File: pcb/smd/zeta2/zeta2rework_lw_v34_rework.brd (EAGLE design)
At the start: 81 x 50.2 mm, 92 parts, among them IC1 DRV8844PWPR, IC2 DRV8844PWPR, M1 IRLML2502, M2 IRLML2502, M3 IRLML2502, U1 STM32F427VI, U3 ICM-20948, U5 DS18B20U+

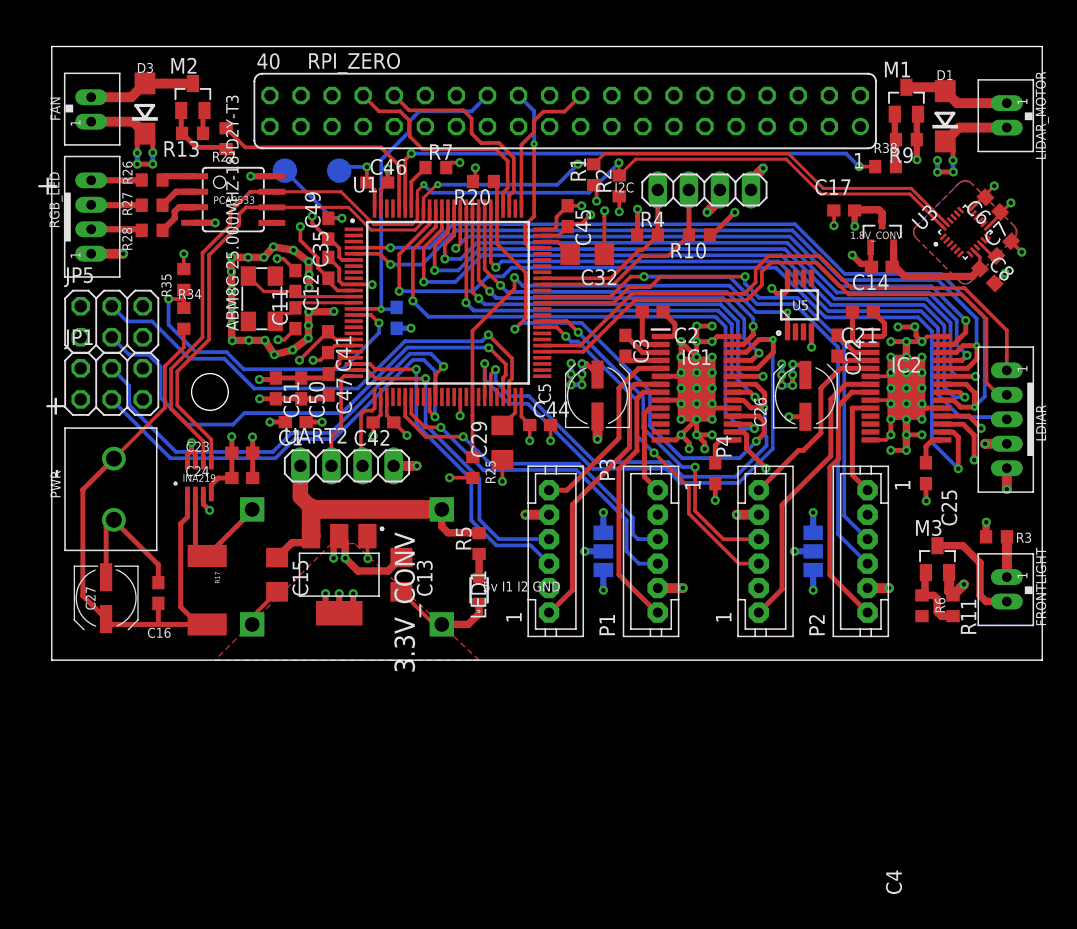
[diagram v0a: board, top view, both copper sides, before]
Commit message: connected power supply
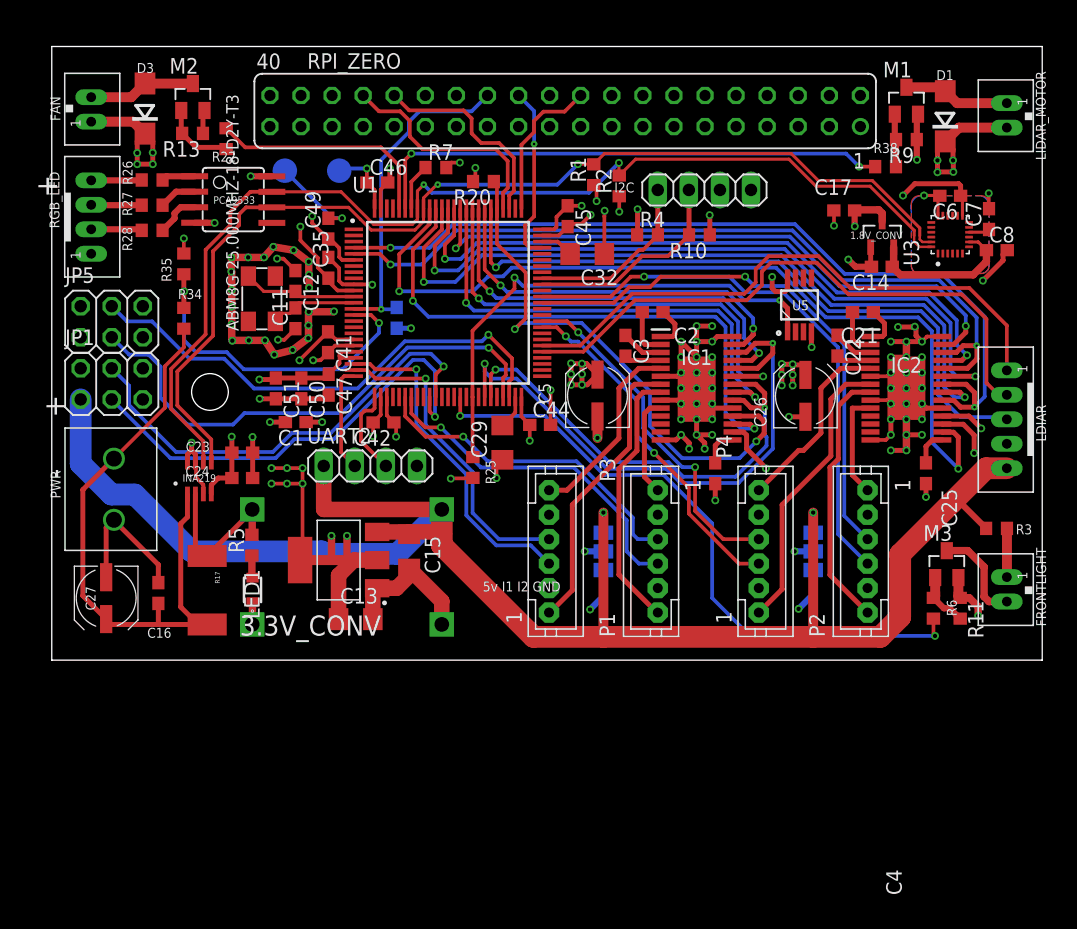
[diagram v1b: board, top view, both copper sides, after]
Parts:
- R5: value 220R -> 390R
- moved R5 18.6 mm to (16.4, 16.4)
- moved LED1 18.5 mm to (16.4, 12.7)
- moved C15 11.0 mm to (29.2, 15.9)
- moved C13 5.21 mm to (24.8, 10.3), turned to 0 degrees
- moved C6 3.55 mm to (73.4, 44.9), turned to 180 degrees
- moved C7 2.69 mm to (76.6, 43.0), turned to 90 degrees
- moved C8 2.26 mm to (77.2, 40.5), turned to 0 degrees
- moved UART2 1.91 mm to (26.0, 22.9)
- moved R35 1.27 mm to (10.8, 39.4)
- moved U3 1.25 mm to (73.4, 41.8), turned to 90 degrees
- moved 3.3V_CONV 1.19 mm to (23.4, 15.2), turned to 180 degrees
- moved R6 0.96 mm to (72.1, 11.2)
- moved M3 0.86 mm to (73.2, 14.8)
- moved R3 0.69 mm to (77.2, 17.8)
- moved R11 0.62 mm to (74.2, 11.2)
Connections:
- net +5V: no longer R5.2
- net +8V: now also R5.2
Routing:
- net +5V: track 49.6 -> 251.7 mm, vias 6 -> 2
- net +3V3: track 97.5 -> 297.8 mm, vias 27 -> 30
- net +8V: track 51.3 -> 161.8 mm
- net PWM_LIGHT: track 1.55 -> 52.8 mm, vias 1 -> 2
- net GND: track 221.5 -> 211.7 mm, vias 111 -> 102
- net +1.8V: track 11.3 -> 12.7 mm
- net M_PWM_LF: track 50.0 -> 48.7 mm
- net N$10: track 5.88 -> 4.60 mm
- net N$9: track 9.12 -> 8.06 mm
- net N$32: track 13.9 -> 12.9 mm
- net N$41: track 13.8 -> 12.9 mm
- net N$24: track 4.46 -> 3.65 mm
- net UART2_RX: track 6.51 -> 7.29 mm
- net SWDIO: track 15.2 -> 14.5 mm
- net N$6: track 3.30 -> 3.98 mm
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- removed copper zone on layer 1, net +3V3
